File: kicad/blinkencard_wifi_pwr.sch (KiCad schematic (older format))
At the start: 15 parts, among them J1 USB_B_Micro, J2 Conn_02x04_Odd_Even, U2 ESP32-WROOM-32, U3 AP7361C-33E, U4 MIC5504-1.2YM5

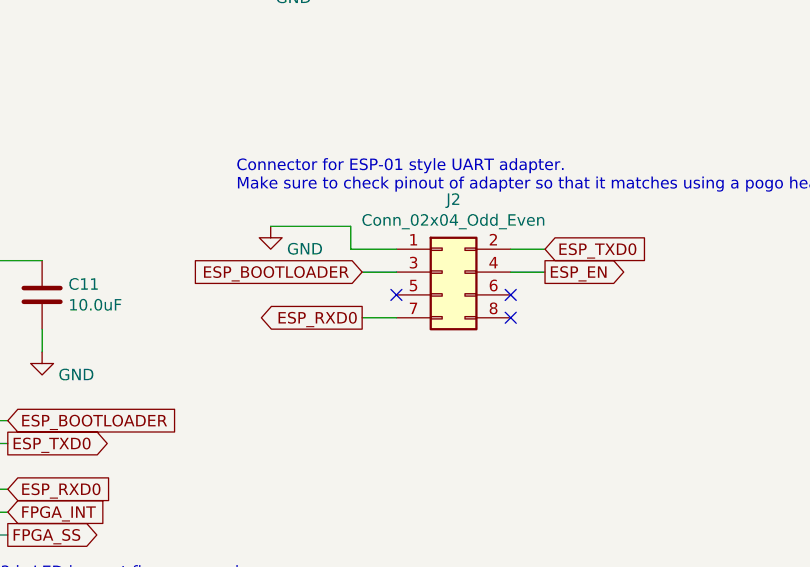
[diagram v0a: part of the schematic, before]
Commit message: Fix RESET and GPIO0 (bootload) on the programming header to match an actual ESP-01 programmer
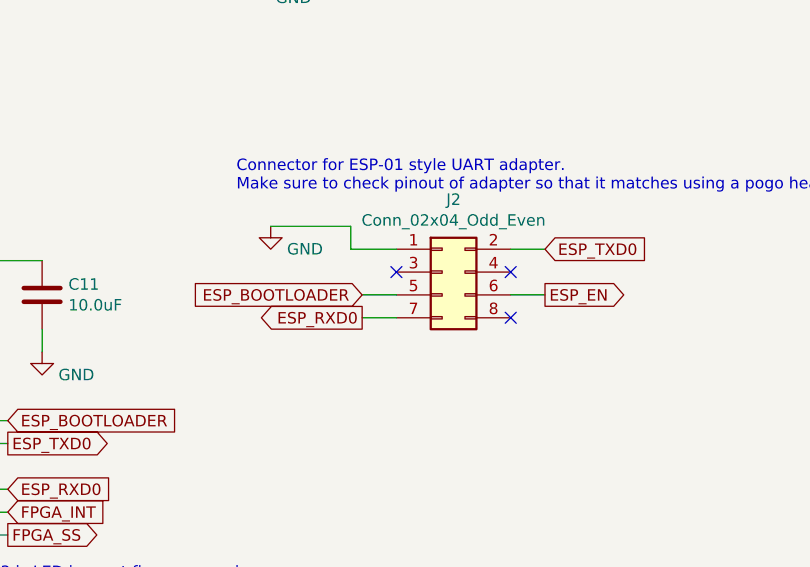
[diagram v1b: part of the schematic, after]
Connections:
- net ESP_BOOTLOADER: now also J2.5 (Pin_5); no longer J2.3 (Pin_3)
- net ESP_EN: now also J2.6 (Pin_6); no longer J2.4 (Pin_4)
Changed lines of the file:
@@
 	1    0    0    -1
 $EndComp
-Text GLabel 5750 2300 2    50   Output ~ 0
+Text GLabel 5750 2400 2    50   Output ~ 0
 ESP_EN
-Wire Wire Line
-	5750 2300 5600 2300
-NoConn ~ 5600 2400
 NoConn ~ 5600 2500
-Text GLabel 4950 2300 0    50   Input ~ 0
+Text GLabel 4950 2400 0    50   Input ~ 0
 ESP_BOOTLOADER
 Wire Wire Line
@@
 Wire Wire Line
 	4550 2100 4900 2100
-Wire Wire Line
-	4950 2300 5100 2300
-NoConn ~ 5100 2400
 Text Notes 4400 1950 0    50   ~ 0
 Connector for ESP-01 style UART adapter.\nMake sure to check pinout of adapter so that it matches using a pogo header
@@
 Wire Wire Line
 	3200 4450 3400 4450
+Wire Wire Line
+	4950 2400 5100 2400
+NoConn ~ 5100 2300
+NoConn ~ 5600 2300
+Wire Wire Line
+	5600 2400 5750 2400
 $EndSCHEMATC

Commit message: Finish converting to ESP32, start on adding LiPo power
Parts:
- added C16: 10.0uF, Capacitor_SMD:C_0805_2012Metric, symbol Device:C
- added D1: B120-E3, Diode_SMD:D_SMA, symbol Diode:B120-E3
- added D2: LED_Small, LED_SMD:LED_0805_2012Metric, symbol Device:LED_Small
- added J3: Conn_01x02, Connector_JST:JST_PH_S2B-PH-SM4-TB_1x02-1MP_P2.00mm_Horizontal, symbol Connector_Generic:Conn_01x02
- added Q6: DMG2301L, Package_TO_SOT_SMD:SOT-23, symbol Transistor_FET:DMG2301L
- added R18: 1K, Resistor_SMD:R_0603_1608Metric, symbol Device:R_US
- added R7: 100K, Resistor_SMD:R_0603_1608Metric, symbol Device:R_US
- added R9: 10K, Resistor_SMD:R_0603_1608Metric, symbol Device:R_US
- added SW5: SW_SPST, Button_Switch_SMD:SW_SPDT_CK-JS102011SAQN, symbol Switch:SW_SPST
- added U5: MCP73831-2-OT, Package_TO_SOT_SMD:SOT-23-5, symbol Battery_Management:MCP73831-2-OT
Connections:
- net +5V: now also D1.2 (A), Q6.1 (G), R18.2, R7.1, U5.4 (VDD); no longer C12.1, C15.1, U3.1 (VI), U4.1 (VIN), U4.3 (EN)
- net GND: now also C16.2, J3.1 (Pin_1), R7.2, R9.1, U5.2 (VSS)
- new net: D1.1 (K), Q6.2 (S), SW5.1 (A)
- new net: D2.1 (K), U5.1 (STAT)
- new net: R9.2, U5.5 (PROG)
- new net: D2.2 (A), R18.1
- new net +BATT: C16.1, J3.2 (Pin_2), Q6.3 (D), U5.3 (VBAT)
- new net VPP: C12.1, C15.1, SW5.2 (B), U3.1 (VI), U4.1 (VIN), U4.3 (EN)

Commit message: First pass routing complete w/ LiPo charging
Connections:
- net UNSWITCHED_VPP: now reaches D1.1 (K), Q6.2 (S), SW5.1 (A)
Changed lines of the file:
@@
 	1    0    0    -1
 $EndComp
-Wire Wire Line
-	8600 3600 9350 3600
 $Comp
 L power:+BATT #PWR026
@@
 	10250 3600 9950 3600
 Connection ~ 9950 3600
+Wire Wire Line
+	8600 3600 9350 3600
+Text Label 8700 3600 0    50   ~ 0
+UNSWITCHED_VPP
 $EndSCHEMATC

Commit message: Add more sch comments
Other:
- note added: "Connector for ESP-01 style UART adapter.\nIntended to use with a no-pop header during\ndevelopment or pogo pins for production"
- note added: "External/battery power switch. Lifted from\nAdafruit's ESP32 Feather design."
- note added: "ICE40UP5K requires 1.2V core rail up before 3.3V.\nWe fudge this by assuming that the ramp on VPP\ncauses the 1.2V LDO to hit the target voltage before 3.3."
- note removed: "Connector for ESP-01 style UART adapter.\nMake sure to check pinout of adapter so that it matches using a pogo header"
- note removed: "ICE40UP5K requires 1.2V core rail up before 3.3V."
- moved on the sheet: C16, D2, J3, R18, R9, U5
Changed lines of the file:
@@
 Wire Wire Line
 	7700 5400 7700 5200
-Text Notes 6400 4650 0    50   ~ 0
-ICE40UP5K requires 1.2V core rail up before 3.3V.
+Text Notes 7600 6300 0    50   ~ 0
+ICE40UP5K requires 1.2V core rail up before 3.3V.\nWe fudge this by assuming that the ramp on VPP\ncauses the 1.2V LDO to hit the target voltage before 3.3.
 $Comp
 L power:GND #PWR0101
@@
 	1    0    0    -1
 $EndComp
-Text GLabel 5750 2200 2    50   Input ~ 0
-ESP_TXD0
-Text GLabel 4950 2500 0    50   Output ~ 0
-ESP_RXD0
 Wire Wire Line
 	4950 2500 5100 2500
@@
 	1    0    0    -1
 $EndComp
-Text GLabel 5750 2400 2    50   Output ~ 0
-ESP_EN
 NoConn ~ 5600 2500
-Text GLabel 4950 2400 0    50   Input ~ 0
-ESP_BOOTLOADER
 Wire Wire Line
 	4900 2100 4900 2200
@@
 Wire Wire Line
 	4550 2100 4900 2100
-Text Notes 4400 1950 0    50   ~ 0
-Connector for ESP-01 style UART adapter.\nMake sure to check pinout of adapter so that it matches using a pogo header
+Text Notes 4450 1900 0    50   ~ 0
+Connector for ESP-01 style UART adapter.\nIntended to use with a no-pop header during\ndevelopment or pogo pins for production
 $Comp
 L Connector:TestPoint TP1
@@
 L Connector_Generic:Conn_01x02 J3
 U 1 1 5DE8EA4C
-P 11050 1750
-F 0 "J3" H 10968 1425 50  0000 C CNN
-F 1 "Conn_01x02" H 10968 1516 50  0000 C CNN
-F 2 "Connector_JST:JST_PH_S2B-PH-SM4-TB_1x02-1MP_P2.00mm_Horizontal" H 11050 1750 50  0001 C CNN
-F 3 "~" H 11050 1750 50  0001 C CNN
-	1    11050 1750
+P 10100 1700
+F 0 "J3" H 10018 1375 50  0000 C CNN
+F 1 "Conn_01x02" H 10018 1466 50  0000 C CNN
+F 2 "Connector_JST:JST_PH_S2B-PH-SM4-TB_1x02-1MP_P2.00mm_Horizontal" H 10100 1700 50  0001 C CNN
+F 3 "~" H 10100 1700 50  0001 C CNN
+	1    10100 1700
 	1    0    0    1
 $EndComp
 Wire Wire Line
-	10850 1750 10600 1750
-Wire Wire Line
-	10600 1750 10600 1950
+	9900 1700 9650 1700
+Wire Wire Line
+	9650 1700 9650 1900
 $Comp
 L power:GND #PWR0103
 U 1 1 5DE92DA4
-P 10600 1950
-F 0 "#PWR0103" H 10600 1700 50  0001 C CNN
-F 1 "GND" H 10500 1800 50  0000 C CNN
-F 2 "" H 10600 1950 50  0001 C CNN
-F 3 "" H 10600 1950 50  0001 C CNN
-	1    10600 1950
+P 9650 1900
+F 0 "#PWR0103" H 9650 1650 50  0001 C CNN
+F 1 "GND" H 9550 1750 50  0000 C CNN
+F 2 "" H 9650 1900 50  0001 C CNN
+F 3 "" H 9650 1900 50  0001 C CNN
+	1    9650 1900
 	-1   0    0    -1
 $EndComp
@@
 L power:+5V #PWR0104
 U 1 1 5DE98126
-P 7700 2650
-F 0 "#PWR0104" H 7700 2500 50  0001 C CNN
-F 1 "+5V" H 7715 2823 50  0000 C CNN
-F 2 "" H 7700 2650 50  0001 C CNN
-F 3 "" H 7700 2650 50  0001 C CNN
-	1    7700 2650
-	1    0    0    -1
-$EndComp
-Wire Wire Line
-	7700 2650 7700 3400
+P 7700 3150
+F 0 "#PWR0104" H 7700 3000 50  0001 C CNN
+F 1 "+5V" H 7715 3323 50  0000 C CNN
+F 2 "" H 7700 3150 50  0001 C CNN
+F 3 "" H 7700 3150 50  0001 C CNN
+	1    7700 3150
+	1    0    0    -1
+$EndComp
 Connection ~ 7700 3400
 $Comp
@@
 L Battery_Management:MCP73831-2-OT U5
 U 1 1 5DEAD03E
-P 9250 1750
-F 0 "U5" H 9050 2050 50  0000 C CNN
-F 1 "MCP73831-2-OT" H 9600 1450 50  0000 C CNN
-F 2 "Package_TO_SOT_SMD:SOT-23-5" H 9300 1500 50  0001 L CIN
-F 3 "http://ww1.microchip.com/downloads/en/DeviceDoc/20001984g.pdf" H 9100 1700 50  0001 C CNN
-	1    9250 1750
+P 8300 1700
+F 0 "U5" H 8100 2000 50  0000 C CNN
+F 1 "MCP73831-2-OT" H 8650 1400 50  0000 C CNN
+F 2 "Package_TO_SOT_SMD:SOT-23-5" H 8350 1450 50  0001 L CIN
+F 3 "http://ww1.microchip.com/downloads/en/DeviceDoc/20001984g.pdf" H 8150 1650 50  0001 C CNN
+	1    8300 1700
 	1    0    0    -1
 $EndComp
@@
 L power:+BATT #PWR0112
 U 1 1 5DEC5053
-P 10600 1450
-F 0 "#PWR0112" H 10600 1300 50  0001 C CNN
-F 1 "+BATT" H 10615 1623 50  0000 C CNN
-F 2 "" H 10600 1450 50  0001 C CNN
-F 3 "" H 10600 1450 50  0001 C CNN
-	1    10600 1450
-	1    0    0    -1
-$EndComp
-Wire Wire Line
-	10850 1650 10600 1650
-Wire Wire Line
-	10600 1650 10600 1450
+P 9650 1400
+F 0 "#PWR0112" H 9650 1250 50  0001 C CNN
+F 1 "+BATT" H 9665 1573 50  0000 C CNN
+F 2 "" H 9650 1400 50  0001 C CNN
+F 3 "" H 9650 1400 50  0001 C CNN
+	1    9650 1400
+	1    0    0    -1
+$EndComp
+Wire Wire Line
+	9900 1600 9650 1600
+Wire Wire Line
+	9650 1600 9650 1400
 $Comp
 L power:+5V #PWR0113
 U 1 1 5DEC7638
-P 9250 1300
-F 0 "#PWR0113" H 9250 1150 50  0001 C CNN
-F 1 "+5V" H 9265 1473 50  0000 C CNN
-F 2 "" H 9250 1300 50  0001 C CNN
-F 3 "" H 9250 1300 50  0001 C CNN
-	1    9250 1300
-	1    0    0    -1
-$EndComp
-Wire Wire Line
-	9250 1300 9250 1450
+P 8300 1250
+F 0 "#PWR0113" H 8300 1100 50  0001 C CNN
+F 1 "+5V" H 8315 1423 50  0000 C CNN
+F 2 "" H 8300 1250 50  0001 C CNN
+F 3 "" H 8300 1250 50  0001 C CNN
+	1    8300 1250
+	1    0    0    -1
+$EndComp
+Wire Wire Line
+	8300 1250 8300 1400
 $Comp
 L power:GND #PWR0114
 U 1 1 5DEC9660
-P 9250 2300
-F 0 "#PWR0114" H 9250 2050 50  0001 C CNN
-F 1 "GND" H 9400 2200 50  0000 C CNN
-F 2 "" H 9250 2300 50  0001 C CNN
-F 3 "" H 9250 2300 50  0001 C CNN
-	1    9250 2300
+P 8300 2250
+F 0 "#PWR0114" H 8300 2000 50  0001 C CNN
+F 1 "GND" H 8450 2150 50  0000 C CNN
+F 2 "" H 8300 2250 50  0001 C CNN
+F 3 "" H 8300 2250 50  0001 C CNN
+	1    8300 2250
 	-1   0    0    -1
 $EndComp
@@
 L Device:R_US R9
 U 1 1 5DECB7EF
-P 8650 2000
-F 0 "R9" H 8582 1954 50  0000 R CNN
-F 1 "10K" H 8582 2045 50  0000 R CNN
-F 2 "Resistor_SMD:R_0603_1608Metric" V 8690 1990 50  0001 C CNN
-F 3 "~" H 8650 2000 50  0001 C CNN
-	1    8650 2000
+P 7700 1950
+F 0 "R9" H 7632 1904 50  0000 R CNN
+F 1 "10K" H 7632 1995 50  0000 R CNN
+F 2 "Resistor_SMD:R_0603_1608Metric" V 7740 1940 50  0001 C CNN
+F 3 "~" H 7700 1950 50  0001 C CNN
+	1    7700 1950
 	-1   0    0    1
 $EndComp
 Wire Wire Line
-	9250 2050 9250 2150
-Wire Wire Line
-	9250 2150 8650 2150
-Connection ~ 9250 2150
-Wire Wire Line
-	9250 2150 9250 2300
-Wire Wire Line
-	8650 1850 8850 1850
+	8300 2000 8300 2100
+Wire Wire Line
+	8300 2100 7700 2100
+Connection ~ 8300 2100
+Wire Wire Line
+	8300 2100 8300 2250
+Wire Wire Line
+	7700 1800 7900 1800
 $Comp
 L Device:C C16
 U 1 1 5DED3FBB
-P 10150 1800
-F 0 "C16" H 10265 1846 50  0000 L CNN
-F 1 "10.0uF" H 10265 1755 50  0000 L CNN
-F 2 "Capacitor_SMD:C_0805_2012Metric" H 10188 1650 50  0001 C CNN
-F 3 "~" H 10150 1800 50  0001 C CNN
-	1    10150 1800
-	1    0    0    -1
-$EndComp
-Wire Wire Line
-	9650 1650 10150 1650
-Wire Wire Line
-	10150 1650 10600 1650
-Connection ~ 10150 1650
-Connection ~ 10600 1650
+P 9200 1750
+F 0 "C16" H 9315 1796 50  0000 L CNN
+F 1 "10.0uF" H 9315 1705 50  0000 L CNN
+F 2 "Capacitor_SMD:C_0805_2012Metric" H 9238 1600 50  0001 C CNN
+F 3 "~" H 9200 1750 50  0001 C CNN
+	1    9200 1750
+	1    0    0    -1
+$EndComp
+Wire Wire Line
+	8700 1600 9200 1600
+Wire Wire Line
+	9200 1600 9650 1600
+Connection ~ 9200 1600
+Connection ~ 9650 1600
 $Comp
 L power:GND #PWR0115
 U 1 1 5DEE1A99
-P 10150 2050
-F 0 "#PWR0115" H 10150 1800 50  0001 C CNN
-F 1 "GND" H 10050 1900 50  0000 C CNN
-F 2 "" H 10150 2050 50  0001 C CNN
-F 3 "" H 10150 2050 50  0001 C CNN
-	1    10150 2050
+P 9200 2000
+F 0 "#PWR0115" H 9200 1750 50  0001 C CNN
+F 1 "GND" H 9100 1850 50  0000 C CNN
+F 2 "" H 9200 2000 50  0001 C CNN
+F 3 "" H 9200 2000 50  0001 C CNN
+	1    9200 2000
 	-1   0    0    -1
 $EndComp
 Wire Wire Line
-	10150 1950 10150 2050
+	9200 1900 9200 2000
 $Comp
 L Device:LED_Small D2
 U 1 1 5DEE704D
-P 9850 1400
-F 0 "D2" V 9896 1332 50  0000 R CNN
-F 1 "LED_Small" V 9805 1332 50  0000 R CNN
-F 2 "LED_SMD:LED_0805_2012Metric" V 9850 1400 50  0001 C CNN
-F 3 "~" V 9850 1400 50  0001 C CNN
-	1    9850 1400
+P 8900 1350
+F 0 "D2" V 8946 1282 50  0000 R CNN
+F 1 "LED_Small" V 8855 1282 50  0000 R CNN
+F 2 "LED_SMD:LED_0805_2012Metric" V 8900 1350 50  0001 C CNN
+F 3 "~" V 8900 1350 50  0001 C CNN
+	1    8900 1350
 	0    -1   -1   0
 $EndComp
 Wire Wire Line
-	9650 1850 9850 1850
-Wire Wire Line
-	9850 1850 9850 1500
+	8700 1800 8900 1800
+Wire Wire Line
+	8900 1800 8900 1450
 $Comp
 L Device:R_US R18
 U 1 1 5DEEAB8F
-P 9850 1050
-F 0 "R18" H 9782 1004 50  0000 R CNN
-F 1 "1K" H 9782 1095 50  0000 R CNN
-F 2 "Resistor_SMD:R_0603_1608Metric" V 9890 1040 50  0001 C CNN
-F 3 "~" H 9850 1050 50  0001 C CNN
-	1    9850 1050
+P 8900 1000
+F 0 "R18" H 8832 954 50  0000 R CNN
+F 1 "1K" H 8832 1045 50  0000 R CNN
+F 2 "Resistor_SMD:R_0603_1608Metric" V 8940 990 50  0001 C CNN
+F 3 "~" H 8900 1000 50  0001 C CNN
+	1    8900 1000
 	-1   0    0    1
 $EndComp
@@
 L power:+5V #PWR0116
 U 1 1 5DEEAF38
-P 9850 800
-F 0 "#PWR0116" H 9850 650 50  0001 C CNN
-F 1 "+5V" H 9865 973 50  0000 C CNN
-F 2 "" H 9850 800 50  0001 C CNN
-F 3 "" H 9850 800 50  0001 C CNN
-	1    9850 800
-	1    0    0    -1
-$EndComp
-Wire Wire Line
-	9850 800  9850 900
-Wire Wire Line
-	9850 1200 9850 1300
+P 8900 750
+F 0 "#PWR0116" H 8900 600 50  0001 C CNN
+F 1 "+5V" H 8915 923 50  0000 C CNN
+F 2 "" H 8900 750 50  0001 C CNN
+F 3 "" H 8900 750 50  0001 C CNN
+	1    8900 750
+	1    0    0    -1
+$EndComp
+Wire Wire Line
+	8900 750  8900 850
+Wire Wire Line
+	8900 1150 8900 1250
 $Comp
 L Switch:SW_SPST SW5
@@
 Text Label 8700 3600 0    50   ~ 0
 UNSWITCHED_VPP
+Wire Wire Line
+	7700 3150 7700 3400
+Wire Notes Line
+	7500 2850 10500 2850
+Wire Notes Line
+	10500 2850 10500 4400
+Wire Notes Line
+	10500 4400 7500 4400
+Wire Notes Line
+	7500 4400 7500 2850
+Text Notes 8500 4000 0    50   ~ 0
+External/battery power switch. Lifted from\nAdafruit's ESP32 Feather design.
+Text GLabel 5750 2400 2    50   Output ~ 0
+ESP_EN
+Text GLabel 5750 2200 2    50   Input ~ 0
+ESP_TXD0
+Text GLabel 4950 2500 0    50   Output ~ 0
+ESP_RXD0
+Text GLabel 4950 2400 0    50   Input ~ 0
+ESP_BOOTLOADER
+Wire Notes Line
+	6400 1550 6400 2600
+Wire Notes Line
+	6400 2600 4150 2600
+Wire Notes Line
+	4150 2600 4150 1550
+Wire Notes Line
+	4150 1550 6400 1550
+Wire Notes Line
+	3800 650  4800 650
+Wire Notes Line
+	4800 650  4800 1000
+Wire Notes Line
+	4800 1000 3800 1000
+Wire Notes Line
+	3800 1000 3800 650
 $EndSCHEMATC

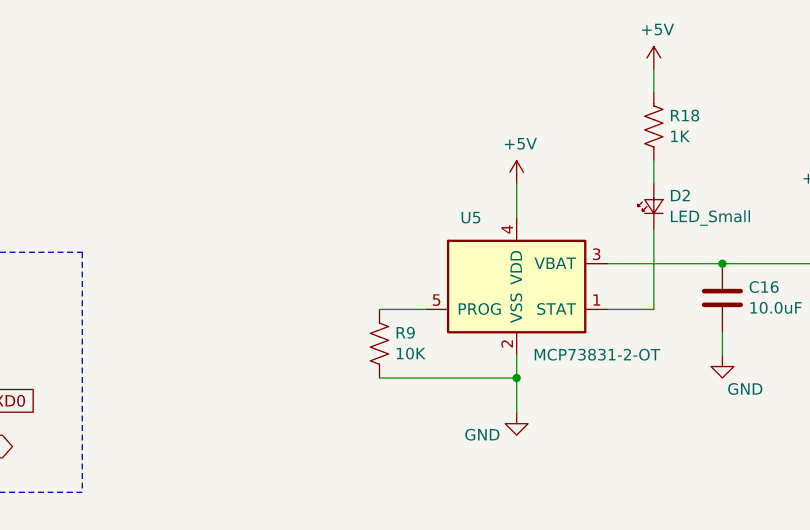
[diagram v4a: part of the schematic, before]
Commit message: Add cap across 5V for charger
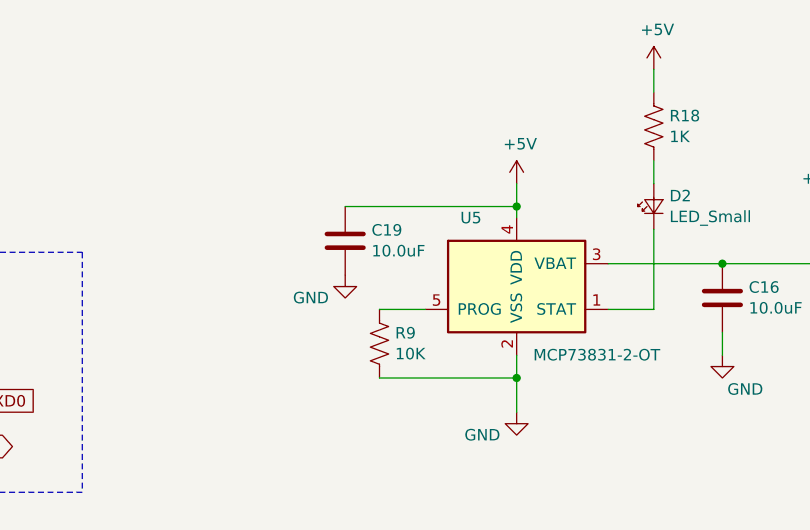
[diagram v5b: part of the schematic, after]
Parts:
- added C19: 10.0uF, Capacitor_SMD:C_0805_2012Metric, symbol Device:C
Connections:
- net +5V: now also C19.1
- net GND: now also C19.2
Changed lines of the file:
@@
 $EndComp
 Wire Wire Line
-	8300 1250 8300 1400
+	8300 1250 8300 1350
 $Comp
 L power:GND #PWR0114
@@
 Wire Notes Line
 	3800 1000 3800 650
+$Comp
+L Device:C C19
+U 1 1 5DFB6317
+P 7550 1500
+F 0 "C19" H 7665 1546 50  0000 L CNN
+F 1 "10.0uF" H 7665 1455 50  0000 L CNN
+F 2 "Capacitor_SMD:C_0805_2012Metric" H 7588 1350 50  0001 C CNN
+F 3 "~" H 7550 1500 50  0001 C CNN
+	1    7550 1500
+	1    0    0    -1
+$EndComp
+$Comp
+L power:GND #PWR028
+U 1 1 5DFB6E84
+P 7550 1650
+F 0 "#PWR028" H 7550 1400 50  0001 C CNN
+F 1 "GND" H 7700 1550 50  0000 C CNN
+F 2 "" H 7550 1650 50  0001 C CNN
+F 3 "" H 7550 1650 50  0001 C CNN
+	1    7550 1650
+	-1   0    0    -1
+$EndComp
+Wire Wire Line
+	7550 1350 8300 1350
+Connection ~ 8300 1350
+Wire Wire Line
+	8300 1350 8300 1400
 $EndSCHEMATC

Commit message: v2.0 release - clean silk, add order number placeholder for JLCPCB, add MFG PN in components for BOM, add BOM, add STEP, generate fab outputs
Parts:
- C10:  mfg_part (none) -> CL10F104ZO8NNNC
- C11, C14, C15, C16, C17, C19:  mfg_part (none) -> CL21A106KQCLRNC
- C12, C13:  mfg_part (none) -> CL21B105KOFNNNG
- D1:  mfg_part (none) -> B120-E3/61T
- D2:  mfg_part (none) -> LTST-S220GKT
- J1:  mfg_part (none) -> 105017-0001
- J2:  mfg_part (none) -> 54202-S0804LF
- J3:  mfg_part (none) -> S2B-PH-SM4-TB(LF)(SN)
- Q6:  mfg_part (none) -> DMG2301L-7
- R18:  mfg_part (none) -> RC0603JR-071KL
- R6, R9:  mfg_part (none) -> RC0603JR-0710KL
- R7:  mfg_part (none) -> RC0603JR-07100KL
- SW5:  mfg_part (none) -> JS102011SAQN
- TP1, TP2:  mfg_part (none) -> NP
- U2:  mfg_part (none) -> ESP32-WROOM-32D
- U3:  mfg_part (none) -> AP7361C-33E-13
- U4:  mfg_part (none) -> MIC5504-1.2YM5
- U5:  mfg_part (none) -> MCP73831T-2ATI/OT
